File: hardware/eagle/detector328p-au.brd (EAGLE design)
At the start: 40 x 70 mm, 68 parts, among them K1 SRD-05VDC-SL-C, Q1 BSS123, Q2 16MHz, T1 BC817, T2 BC817, T3 BC817, U1 ATMEGA328P-AU

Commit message: hardware/eagle: added 3 push buttons
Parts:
- added B1, B2, B3: (no value), detector:B3F-10XX
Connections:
- new net N$49: B1.1, B1.2, U1.32
- new net N$50: B2.1, B2.2, U1.1
- new net N$51: B3.1, B3.2, U1.9
- net GND: now also B1.3, B1.4, B2.3, B2.4, B3.3, B3.4
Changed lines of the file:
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@@
 <?xml version="1.0" encoding="utf-8"?>
 <!DOCTYPE eagle SYSTEM "eagle.dtd">
-<eagle version="7.1.0">
+<eagle version="7.6.0">
 <drawing>
 <settings>
@@
 <attribute name="VALUE" x="13.081" y="42.926" size="1.27" layer="27" ratio="10" rot="R270"/>
 </element>
+<element name="B1" library="detector" package="B3F-10XX" value="" x="-16.256" y="5.588">
+<attribute name="OC_NEWARK" value="36M3542" x="-16.256" y="5.588" size="1.778" layer="27" display="off"/>
+<attribute name="MF" value="" x="-16.256" y="5.588" size="1.778" layer="27" display="off"/>
+<attribute name="OC_FARNELL" value="176432" x="-16.256" y="5.588" size="1.778" layer="27" display="off"/>
+<attribute name="MPN" value="B3F-1000" x="-16.256" y="5.588" size="1.778" layer="27" display="off"/>
+</element>
+<element name="B2" library="detector" package="B3F-10XX" value="" x="-26.924" y="5.588">
+<attribute name="OC_NEWARK" value="36M3542" x="-26.924" y="5.588" size="1.778" layer="27" display="off"/>
+<attribute name="MF" value="" x="-26.924" y="5.588" size="1.778" layer="27" display="off"/>
+<attribute name="OC_FARNELL" value="176432" x="-26.924" y="5.588" size="1.778" layer="27" display="off"/>
+<attribute name="MPN" value="B3F-1000" x="-26.924" y="5.588" size="1.778" layer="27" display="off"/>
+</element>
+<element name="B3" library="detector" package="B3F-10XX" value="" x="-37.592" y="5.588">
+<attribute name="OC_NEWARK" value="36M3542" x="-37.592" y="5.588" size="1.778" layer="27" display="off"/>
+<attribute name="MF" value="" x="-37.592" y="5.588" size="1.778" layer="27" display="off"/>
+<attribute name="OC_FARNELL" value="176432" x="-37.592" y="5.588" size="1.778" layer="27" display="off"/>
+<attribute name="MPN" value="B3F-1000" x="-37.592" y="5.588" size="1.778" layer="27" display="off"/>
+</element>
 </elements>
 <signals>
@@
 <wire x1="12.87" y1="39.2" x2="12.954" y2="39.116" width="0.254" layer="1"/>
 <wire x1="12.954" y1="39.116" x2="16.002" y2="39.116" width="0.254" layer="1"/>
+<contactref element="B1" pad="3" route="any" routetag="1.S"/>
+<contactref element="B1" pad="4" route="any" routetag="1.S"/>
+<contactref element="B2" pad="3" route="any" routetag="1.S"/>
+<contactref element="B2" pad="4" route="any" routetag="1.S"/>
+<contactref element="B3" pad="3" route="any" routetag="1.S"/>
+<contactref element="B3" pad="4" route="any" routetag="1.S"/>
+<wire x1="-13.0048" y1="3.3274" x2="1.69" y2="37.084" width="0" layer="19" extent="1-1"/>
+<wire x1="-23.6728" y1="3.3274" x2="-19.5072" y2="3.3274" width="0" layer="19" extent="1-1"/>
+<wire x1="-34.3408" y1="3.3274" x2="-30.1752" y2="3.3274" width="0" layer="19" extent="1-1"/>
 </signal>
 <signal name="VCC">
@@
 <wire x1="18.034" y1="38.608" x2="16.002" y2="36.576" width="0.254" layer="16"/>
 </signal>
+<signal name="N$49">
+<contactref element="U1" pad="32"/>
+<contactref element="B1" pad="1" route="any" routetag="1.P"/>
+<contactref element="B1" pad="2" route="any" routetag="1.P"/>
+<wire x1="-13.0048" y1="7.8486" x2="19.93" y2="43.682" width="0" layer="19" extent="1-1"/>
+</signal>
+<signal name="N$50">
+<contactref element="U1" pad="1"/>
+<contactref element="B2" pad="1" route="any" routetag="1.P"/>
+<contactref element="B2" pad="2" route="any" routetag="1.P"/>
+<wire x1="-23.6728" y1="7.8486" x2="21.33" y2="42.282" width="0" layer="19" extent="1-1"/>
+</signal>
+<signal name="N$51">
+<contactref element="U1" pad="9"/>
+<contactref element="B3" pad="1" route="any" routetag="1.P"/>
+<contactref element="B3" pad="2" route="any" routetag="1.P"/>
+<wire x1="-34.3408" y1="7.8486" x2="28.33" y2="43.682" width="0" layer="19" extent="1-1"/>
+</signal>
 </signals>

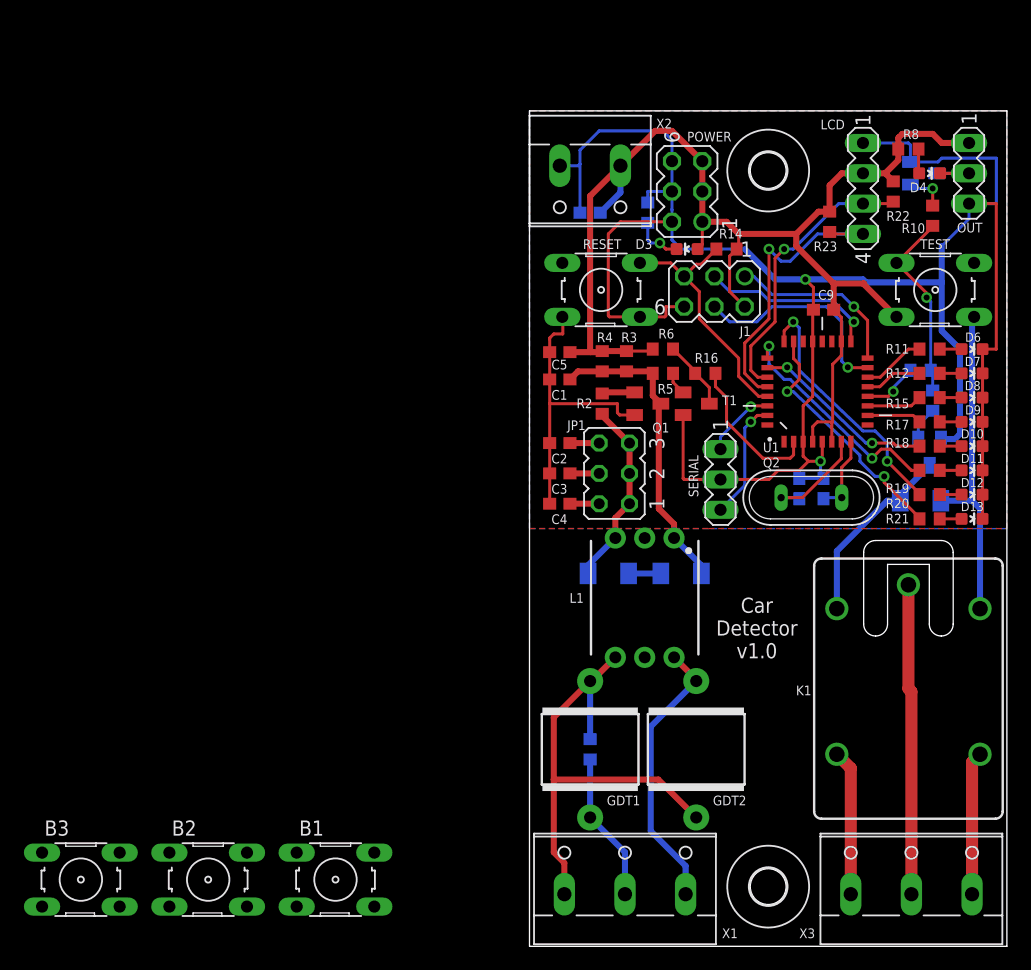
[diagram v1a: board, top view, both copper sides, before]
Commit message: CarDetector v1.1 hardware (3 more button)
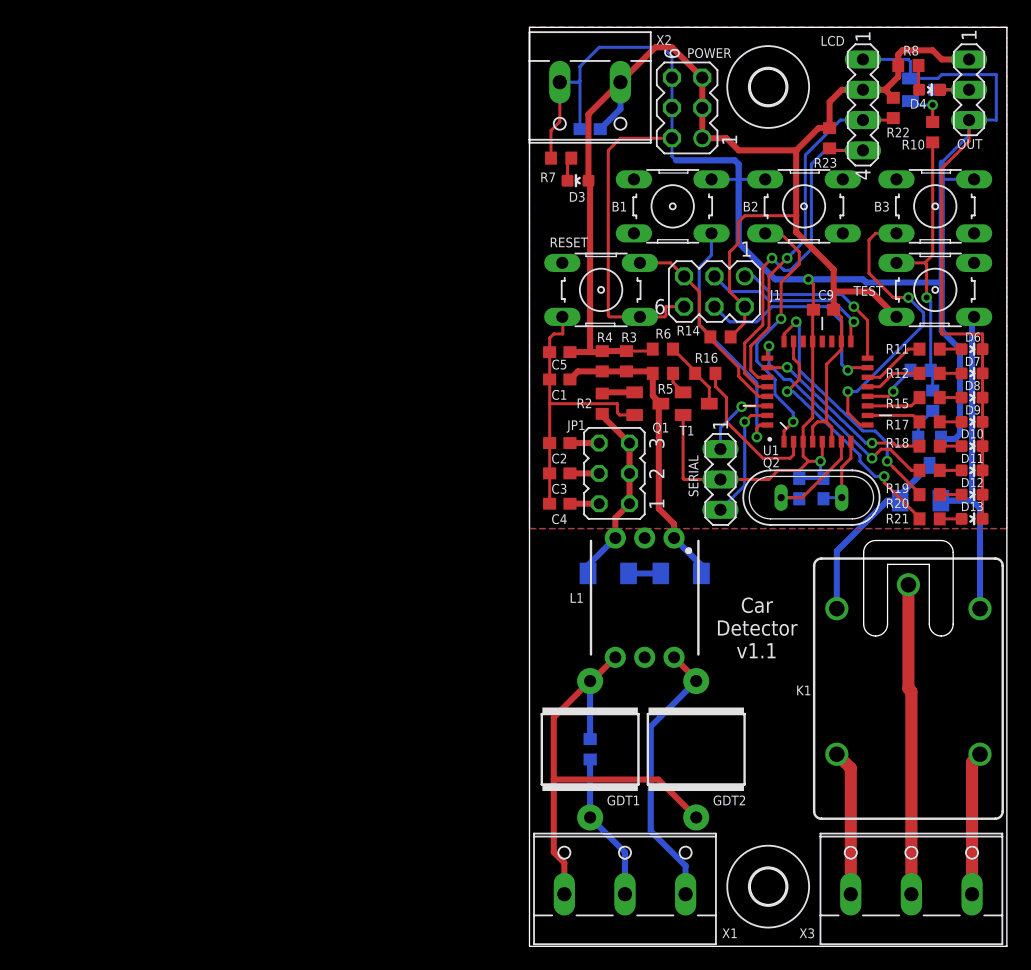
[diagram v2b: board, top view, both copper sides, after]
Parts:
- moved B3 91.1 mm to (34.0, 62.0), turned to 180 degrees
- moved B2 75.3 mm to (23.0, 62.0), turned to 180 degrees
- moved B1 63.1 mm to (12.0, 62.0), turned to 180 degrees
- moved D3 10.8 mm to (4.06, 64.2)
- moved R7 8.57 mm to (2.65, 66.0), flipped to the top, turned to 180 degrees
- moved R14 7.38 mm to (16.0, 51.1)
- moved C6 7.00 mm to (5.08, 68.5)
- moved D4 7.00 mm to (33.5, 71.8)
- moved LCD 7.00 mm to (27.9, 70.5)
- moved OUT 7.00 mm to (36.8, 71.8)
- moved R10 7.00 mm to (33.8, 68.2)
- moved R23 7.00 mm to (25.1, 67.7)
- moved R8 7.00 mm to (31.8, 73.8)
- moved T2 7.00 mm to (33.0, 71.8)
- moved U$2 7.00 mm to (20.0, 72.0)
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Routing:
- net GND: track 205.9 -> 245.4 mm
- net N$51: track 0.00 -> 24.8 mm, vias 0 -> 2
- net N$50: track 0.00 -> 22.4 mm, vias 0 -> 2
- net N$49: track 0.00 -> 21.2 mm, vias 0 -> 1
- net VCC: track 138.1 -> 158.4 mm
- net N$47: track 16.3 -> 23.7 mm
- net N$45: track 23.7 -> 30.2 mm
- net N$44: track 25.7 -> 32.2 mm
- net N$30: track 21.2 -> 17.5 mm
- net N$22: track 4.18 -> 2.02 mm, vias 1 -> 0
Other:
- board size 40 x 70 mm -> 40 x 77 mm
- board text added: "Car Detector v1.1"
- board text removed: "Car Detector v1.0"

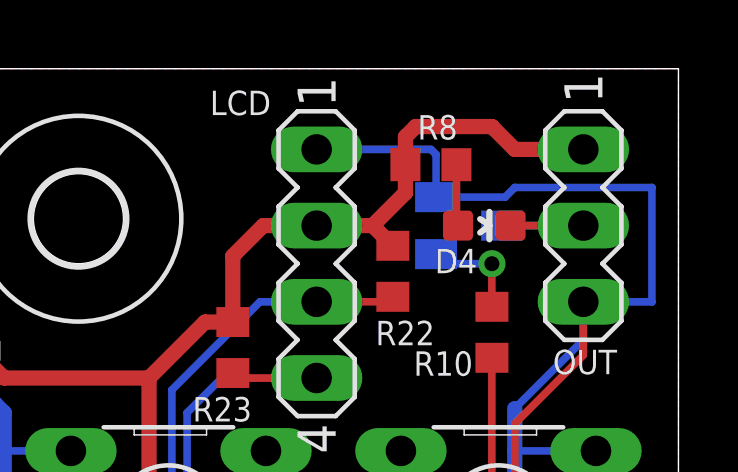
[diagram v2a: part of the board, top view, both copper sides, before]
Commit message: Fix: detector_t85-pu: T2 10K pull-up, Zener 5,1V -> 20V
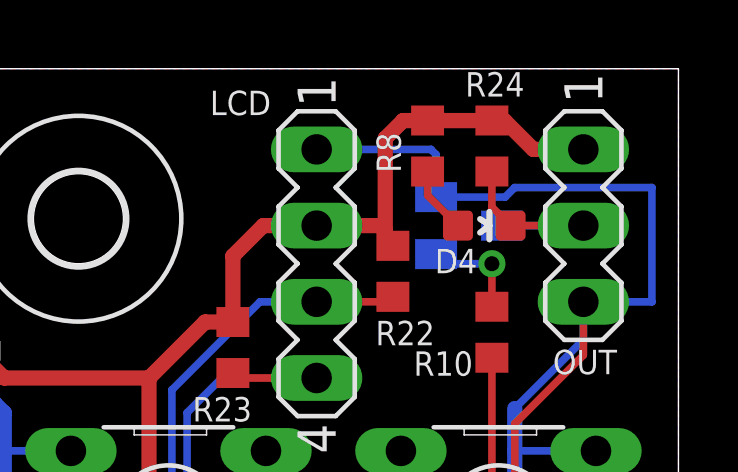
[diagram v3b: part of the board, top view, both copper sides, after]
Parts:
- added R24: 10K, resistor:R0603
- D1, D2: value 5.1V 0.5W -> 20V 0.5W
- moved R8 0.63 mm to (31.6, 74.4), turned to 90 degrees
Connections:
- net N$23: now also R24.1
- net VCC: now also R24.2
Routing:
- net N$23: track 5.13 -> 7.20 mm
- net VCC: track 158.4 -> 159.2 mm
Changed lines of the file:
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@@
 <attribute name="VALUE" x="25.273" y="55.245" size="1.27" layer="27" rot="R180"/>
 </element>
-<element name="D1" library="diode" package="SOD80C" value="5.1V 0.5W" x="12.7" y="31.242" smashed="yes" rot="MR180">
+<element name="D1" library="diode" package="SOD80C" value="20V 0.5W" x="12.7" y="31.242" smashed="yes" rot="MR180">
 <attribute name="NAME" x="13.208" y="29.083" size="0.8128" layer="26" font="vector" rot="MR0"/>
 <attribute name="VALUE" x="11.176" y="33.655" size="1.27" layer="28" rot="MR180"/>
@@
 <attribute name="VALUE" x="36.068" y="34.7345" size="0.4064" layer="27"/>
 </element>
-<element name="D2" library="diode" package="SOD80C" value="5.1V 0.5W" x="6.604" y="31.242" smashed="yes" rot="MR0">
+<element name="D2" library="diode" package="SOD80C" value="20V 0.5W" x="6.604" y="31.242" smashed="yes" rot="MR0">
 <attribute name="NAME" x="7.112" y="29.083" size="0.8128" layer="26" font="vector" rot="MR0"/>
 <attribute name="VALUE" x="8.128" y="28.829" size="1.27" layer="28" rot="MR0"/>
@@
 <attribute name="VALUE" x="3.287" y="67.945" size="1.27" layer="27" rot="R180"/>
 </element>
-<element name="R8" library="resistor" package="R0603" value="1k" x="31.75" y="73.802" smashed="yes" rot="R180">
-<attribute name="NAME" x="32.639" y="75.453" size="0.8128" layer="25" font="vector" rot="R180"/>
-<attribute name="VALUE" x="32.385" y="75.707" size="1.27" layer="27" rot="R180"/>
+<element name="R8" library="resistor" package="R0603" value="1k" x="31.638" y="74.422" smashed="yes" rot="R90">
+<attribute name="NAME" x="30.749" y="73.533" size="0.8128" layer="25" font="vector" rot="R90"/>
+<attribute name="VALUE" x="33.543" y="73.787" size="1.27" layer="27" rot="R90"/>
 </element>
 <element name="R9" library="resistor" package="R0603" value="4k7" x="33.782" y="45.72" smashed="yes" rot="MR90">
@@
 <attribute name="NAME" x="30.19" y="62.381" size="0.8128" layer="25" font="vector" ratio="10" rot="R180"/>
 <attribute name="VALUE" x="37.048" y="67.08" size="1.27" layer="27" ratio="10" rot="R180"/>
+</element>
+<element name="R24" library="resistor" package="R0603" value="10K" x="33.782" y="74.422" smashed="yes" rot="R90">
+<attribute name="NAME" x="32.893" y="76.073" size="0.8128" layer="25" font="vector"/>
+<attribute name="VALUE" x="35.687" y="73.787" size="1.27" layer="27" rot="R90"/>
 </element>
 </elements>
@@
 <wire x1="26.162" y1="71.77" x2="25.146" y2="70.754" width="0.508" layer="1"/>
 <wire x1="25.146" y1="70.754" x2="25.146" y2="68.556" width="0.508" layer="1"/>
-<wire x1="30.48" y1="71.096" x2="29.806" y2="71.77" width="0.508" layer="1"/>
-<wire x1="29.806" y1="71.77" x2="27.94" y2="71.77" width="0.508" layer="1"/>
-<wire x1="36.83" y1="74.31" x2="34.544" y2="74.31" width="0.508" layer="1"/>
-<wire x1="34.544" y1="74.31" x2="33.782" y2="75.072" width="0.508" layer="1"/>
-<wire x1="33.782" y1="75.072" x2="31.242" y2="75.072" width="0.508" layer="1"/>
-<wire x1="31.242" y1="75.072" x2="30.9" y2="74.73" width="0.508" layer="1"/>
-<wire x1="30.9" y1="74.73" x2="30.9" y2="73.802" width="0.508" layer="1"/>
 <wire x1="22.352" y1="66.69" x2="24.218" y2="68.556" width="0.508" layer="1"/>
 <wire x1="24.218" y1="68.556" x2="25.146" y2="68.556" width="0.508" layer="1"/>
-<wire x1="29.806" y1="71.77" x2="30.9" y2="72.864" width="0.508" layer="1"/>
-<wire x1="30.9" y1="72.864" x2="30.9" y2="73.802" width="0.508" layer="1"/>
 <contactref element="K1" pad="2"/>
 <contactref element="D5" pad="C"/>
@@
 <wire x1="25.33" y1="43.504" x2="25.33" y2="42.282" width="0.254" layer="1"/>
 <wire x1="24.13" y1="43.942" x2="24.892" y2="43.942" width="0.254" layer="1"/>
+<contactref element="R24" pad="2"/>
+<wire x1="30.48" y1="71.096" x2="30.226" y2="71.096" width="0.508" layer="1"/>
+<wire x1="30.226" y1="71.096" x2="30.226" y2="71.628" width="0.508" layer="1"/>
+<wire x1="30.226" y1="71.628" x2="30.226" y2="74.676" width="0.508" layer="1"/>
+<wire x1="30.226" y1="74.676" x2="30.822" y2="75.272" width="0.508" layer="1"/>
+<wire x1="30.822" y1="75.272" x2="31.638" y2="75.272" width="0.508" layer="1"/>
+<wire x1="36.83" y1="74.31" x2="35.164" y2="74.31" width="0.508" layer="1"/>
+<wire x1="35.164" y1="74.31" x2="34.202" y2="75.272" width="0.508" layer="1"/>
+<wire x1="34.202" y1="75.272" x2="33.782" y2="75.272" width="0.508" layer="1"/>
+<wire x1="31.638" y1="75.272" x2="33.782" y2="75.272" width="0.508" layer="1"/>
+<wire x1="27.94" y1="71.77" x2="30.084" y2="71.77" width="0.508" layer="1"/>
+<wire x1="30.084" y1="71.77" x2="30.226" y2="71.628" width="0.508" layer="1"/>
 </signal>
 <signal name="FREQ">
@@
 <wire x1="34.405" y1="71.77" x2="36.83" y2="71.77" width="0.254" layer="1"/>
 <wire x1="34.12" y1="71.77" x2="36.83" y2="71.77" width="0.254" layer="16"/>
+<contactref element="R24" pad="1"/>
+<wire x1="33.782" y1="73.572" x2="33.782" y2="72.393" width="0.254" layer="1"/>
+<wire x1="33.782" y1="72.393" x2="34.405" y2="71.77" width="0.254" layer="1"/>
 </signal>
 <signal name="N$24">
@@
 <contactref element="R8" pad="1"/>
 <wire x1="32.651" y1="71.77" x2="32.6" y2="71.821" width="0.254" layer="1"/>
-<wire x1="32.6" y1="71.821" x2="32.6" y2="73.802" width="0.254" layer="1"/>
+<wire x1="31.638" y1="73.572" x2="31.638" y2="72.783" width="0.254" layer="1"/>
+<wire x1="31.638" y1="72.783" x2="32.651" y2="71.77" width="0.254" layer="1"/>
 </signal>
 <signal name="N$27">

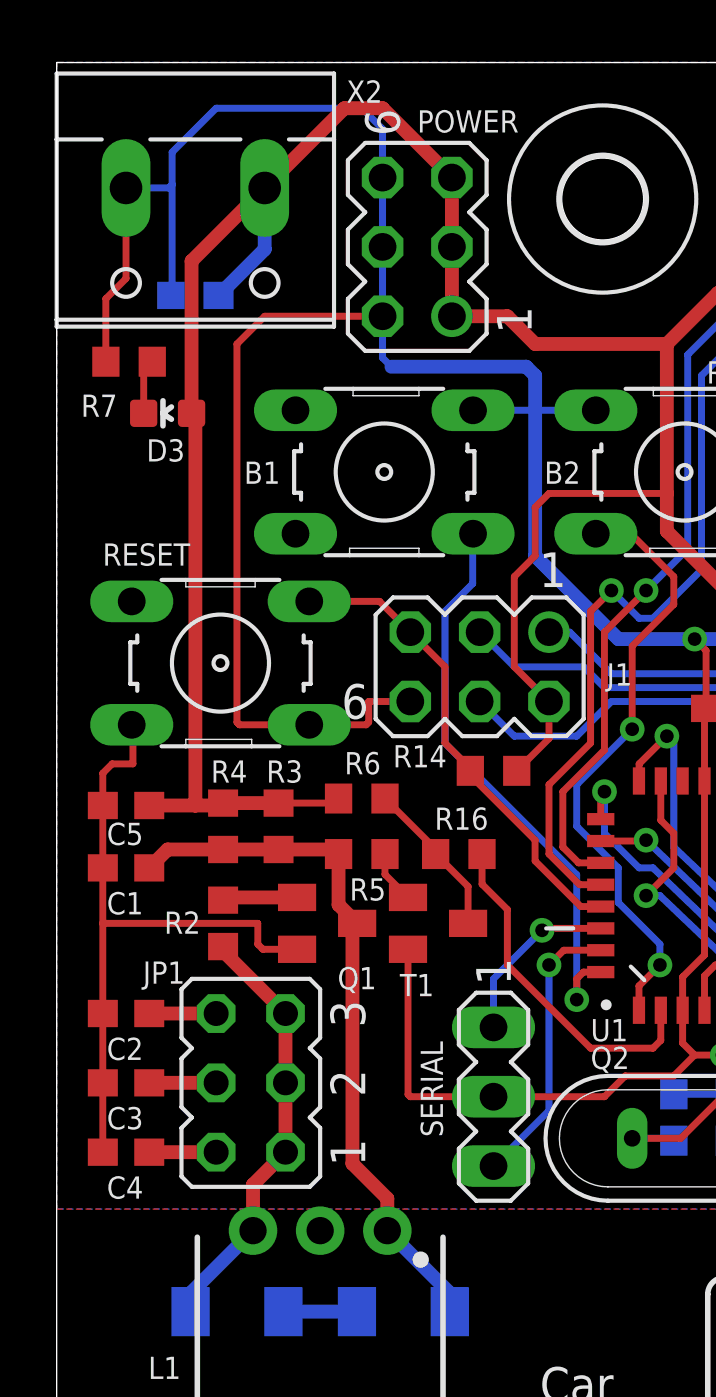
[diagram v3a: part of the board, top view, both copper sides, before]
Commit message: C1: 1206; C2,C3,C4: 0805; Power polarity signs
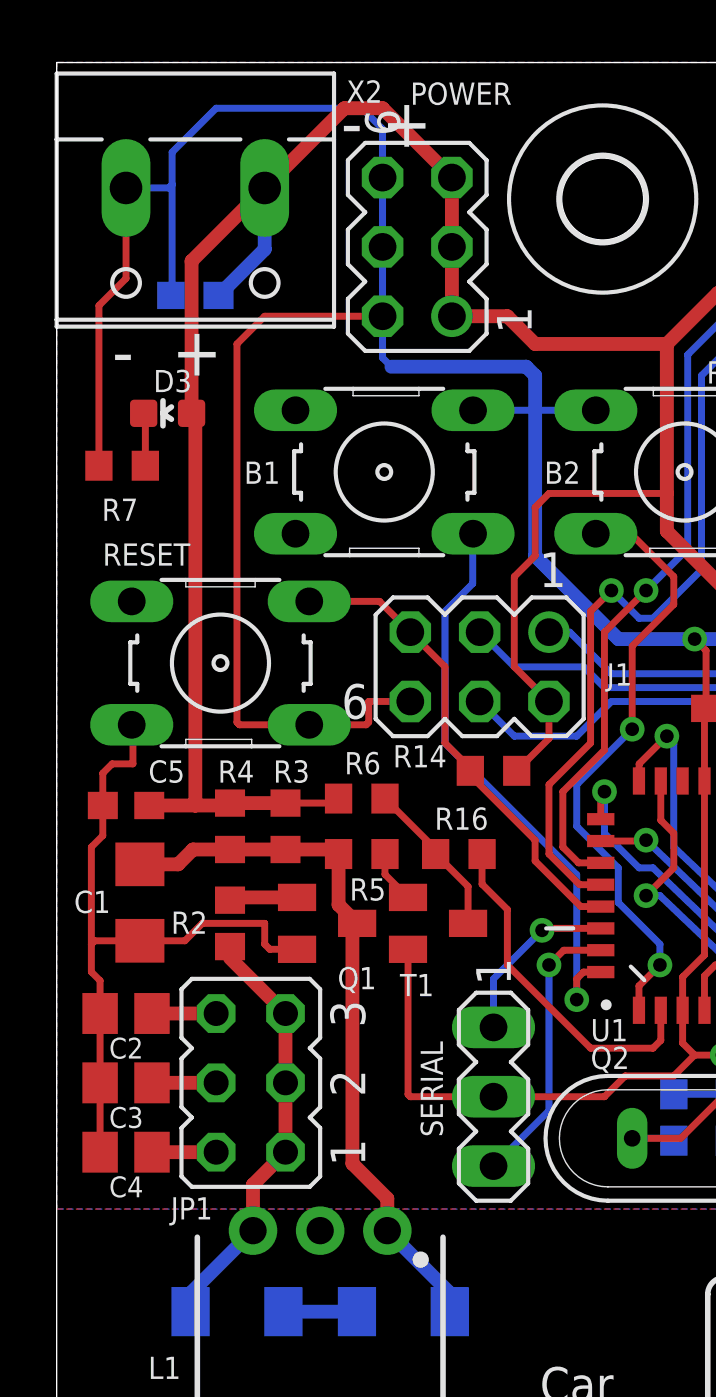
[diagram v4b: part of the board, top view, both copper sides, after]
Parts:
- C1: device resistor:C0603 -> resistor:C1206
- C2, C3, C4: device resistor:C0603 -> resistor:C0805
- moved R7 3.82 mm to (2.40, 62.2)
- moved C1 1.37 mm to (3.05, 46.2), turned to 270 degrees
- moved R2 0.25 mm to (6.35, 45.5)
- moved R3 0.25 mm to (8.38, 49.0)
- moved R4 0.25 mm to (6.35, 49.0)
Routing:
- net GND: track 245.4 -> 250.4 mm
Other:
- board text added: "- +"
